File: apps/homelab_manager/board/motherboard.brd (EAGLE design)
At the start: 100 x 80 mm, 39 parts, among them X1 22-23-2021

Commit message: Adding components
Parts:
- removed JP8: UI, pinhead:1X10
- added C3: 100n, rcl:C0805
- added C5: 10u, rcl:C0805
- added C6: 100u, rcl:C0805
- added JP10: LED, pinhead:1X01
- added JP11: 5V, pinhead:1X01
- added JP9: (no value), pinhead:1X11
- added R16: 330, rcl:R0805
- added R17: 5k, rcl:R0805
- added R18: 1k, rcl:R0805
- added R19: 100k, rcl:R0805
- added U$8: MGSF1N03L, bzd:SOT23_3_PIN
- added U$9: LD1117, bzd:SOT223_3_PIN
- R15: value 20k -> 5k
- moved R15 92.1 mm to (85.1, 15.2)
- moved C1 87.6 mm to (77.5, 14.0)
- moved U$2 81.0 mm to (77.5, 33.0)
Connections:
- removed net N$6: C1.1, R15.2, U$2.B1, U$2.B2
- new net 5V: C3.1, C6.1, JP11.1, U$2.A1, U$2.A2, U$2.H1, U$9.P$2
- new net GND_LED: JP9.11, R16.2
- new net LED: JP10.1, R18.1, R19.2
- new net N$14: R16.1, U$8.P$3
- new net N$7: JP9.9
- new net N$8: R18.2, U$8.P$1
- new net VOUT_GAZ: C1.1, R15.2, R17.1, U$1.PIN_22
- net 3.3V: now also JP9.1; no longer JP8.1, JP8.9
- net 7V: now also C5.1, U$9.P$3
- net EINK_BUSY: now also JP9.8; no longer JP8.8
- net EINK_DC: now also JP9.6; no longer JP8.6
- net EINK_RST: now also JP9.7; no longer JP8.7
- net GND: now also C3.2, C5.2, C6.2, JP9.2, R19.1, U$8.P$2, U$9.P$1; no longer JP8.2
- net N$5: now also R17.2, U$2.B1, U$2.B2; no longer U$2.A1, U$2.A2, U$2.H1
- net SPI_CLK: now also JP9.4; no longer JP8.4
- net SPI_CS0: now also JP9.5; no longer JP8.5
- net SPI_MOSI: now also JP9.3; no longer JP8.3
- net SWITCH: now also JP9.10; no longer JP8.10
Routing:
- net GND: track 52.1 -> 68.5 mm
- net LED: track 0.00 -> 8.93 mm
- net 5V: track 0.00 -> 6.17 mm
- net 7V: track 15.5 -> 18.4 mm
- net N$8: track 0.00 -> 2.75 mm
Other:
- outline, holes or cut-outs redrawn

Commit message: Started main layout
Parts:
- removed X1: 22-23-2021, con-molex:22-23-2021
- added C7: 100n, rcl:C0805
- added D4: 1N4148, diode:DO-214AC
- added DCIN, RELAY: 22-23-2021, con-molex:22-23-2021
- added JP12: HOMELAB, pinhead:1X01
- added R21, R24: 100k, rcl:R0805
- added R23: 1k, rcl:R0805
- added U$10: TMP101, bzd:SOT23_6_PIN
- added U$11: MGSF1N03L, bzd:SOT23_3_PIN
- moved R15 62.0 mm to (34.3, 50.8), flipped to the bottom
- moved JP9 60.6 mm to (35.6, 5.08), turned to 0 degrees
- moved C1 57.4 mm to (30.5, 47.0), flipped to the bottom
- moved R14 55.7 mm to (52.1, 5.08)
- moved L3 50.6 mm to (11.7, 23.6), turned to 180 degrees
- moved R17 50.4 mm to (38.1, 47.0), flipped to the bottom
- moved JP6 50.2 mm to (3.81, 25.4), turned to 180 degrees
- moved C3 45.9 mm to (40.6, 50.8), flipped to the bottom
- moved U$4 44.5 mm to (12.7, 26.7), turned to 180 degrees
- moved C11 44.1 mm to (8.89, 27.2), turned to 90 degrees
- moved R9 43.8 mm to (6.35, 27.9), turned to 90 degrees
- moved C10 43.1 mm to (17.8, 27.9), turned to 270 degrees
- moved R18 42.3 mm to (65.3, 25.5)
- moved JP10 42.3 mm to (61.5, 25.0)
- moved R16 42.3 mm to (57.9, 27.3)
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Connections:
- new net GND_RELAY: D4.A, RELAY.1, U$11.P$3
- new net HOMELAB_POWER: JP12.1, R23.1, R24.2, U$1.PIN_21
- new net N$13: R23.2, U$11.P$1
- new net TEMPERATURE_ALERT: R21.1, U$1.PIN_25, U$10.3
- net 12V: now also DCIN.2; no longer X1.2
- net 3.3V: now also C7.1, R21.2, U$10.4
- net GND: now also C7.2, DCIN.1, R24.1, U$10.2, U$10.5, U$11.P$2; no longer X1.1
- net I2C_SCL: now also U$10.1
- net I2C_SDA: now also U$10.6
- net LED: now also U$1.PIN_26
- net VIN_REG: now also D4.C, RELAY.2
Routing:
- net HOMELAB_POWER: track 0.00 -> 8.93 mm
- net GND: track 68.5 -> 77.5 mm
- net 3.3V: track 0.00 -> 4.58 mm
- net GND_RELAY: track 0.00 -> 3.29 mm
- net N$13: track 0.00 -> 2.75 mm
- net TEMPERATURE_ALERT: track 0.00 -> 2.41 mm
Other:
- board size 100 x 80 mm -> 74.6 x 55.9 mm

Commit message: Updated bazelisk + bazel
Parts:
- removed DCIN: 22-23-2021, con-molex:22-23-2021
- added DC_12V: DC_POWER_2.1MM, bzd:DC_POWER_2.1MM
- moved JP2 11.0 mm to (20.2, 38.2)
- moved R4 11.0 mm to (20.2, 42.0)
- moved U$3 11.0 mm to (17.4, 40.5)
- moved C2 11.0 mm to (15.6, 39.0)
- moved R3 11.0 mm to (16.9, 45.8)
- moved U$1 1.49 mm to (38.6, 32.9)
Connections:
- net 12V: now also DC_12V.1; no longer DCIN.2
- net GND: now also DC_12V.2, DC_12V.3; no longer DCIN.1

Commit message: motherboard (wip)
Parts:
- added JP8: SWITCH_LED, pinhead:1X03
- added RELAY1: 22-23-2021, con-molex:22-23-2021
- added U$12, U$13: SCREW_TERMINAL, bzd:SCREW_TERMINAL
- added U$7: RELAY_SONGLE, bzd:RELAY_SONGLE
- JP9: value (none) -> UI
- moved JP9 70.3 mm to (37.9, 75.4)
- moved JP4 54.2 mm to (18.0, 28.3)
- moved JP7 53.9 mm to (19.6, 36.9)
- moved R10 53.9 mm to (23.7, 28.9)
- moved R11 53.9 mm to (23.7, 33.4)
- moved R12 53.9 mm to (19.0, 40.7)
- moved R13 53.9 mm to (15.7, 41.9)
- moved U$6 53.9 mm to (14.5, 36.9)
- moved D3 53.9 mm to (17.0, 33.6)
- moved R14 53.1 mm to (54.1, 58.2)
- moved U$10 31.9 mm to (46.9, 30.8), flipped to the bottom, turned to 90 degrees
- moved R21 31.0 mm to (42.1, 31.6), flipped to the bottom, turned to 90 degrees
- moved C7 27.3 mm to (43.3, 35.4), flipped to the bottom, turned to 180 degrees
- moved C2 24.9 mm to (16.4, 63.9)
- moved DC_12V 24.9 mm to (-2.79, 76.6)
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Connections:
- removed net N$7: JP9.9
- new net N$15: RELAY1.1, U$7.COMMAND_V-
- new net N$16: U$12.P$2, U$13.P$1
- new net N$17: U$12.P$1, U$7.V-
- new net N$18: U$13.P$2, U$7.NO_V+
- new net N$6: RELAY1.2, U$7.COMMAND_V+
- net 3.3V: now also JP9.9
- net FAN2_SENSE: now also U$1.PIN_21; no longer U$1.PIN_18
- net HOMELAB_POWER: now also U$1.PIN_4; no longer U$1.PIN_21
- net LED: now also U$1.PIN_6; no longer U$1.PIN_26
- net VOUT_CURRENT: now also U$1.PIN_18; no longer U$1.PIN_4
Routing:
- net GND: track 77.5 -> 198.3 mm, vias 6 -> 9
- net VIN_REG: track 14.2 -> 130.7 mm, vias 0 -> 2
- net 7V: track 18.4 -> 94.9 mm, vias 0 -> 2
- net 3.3V: track 4.58 -> 49.4 mm, vias 0 -> 1
- net FAN1_SENSE: track 0.00 -> 38.5 mm, vias 0 -> 1
- net SWITCH: track 0.00 -> 36.8 mm, vias 0 -> 1
- net FAN_SWITCH: track 17.9 -> 53.5 mm, vias 0 -> 2
- net I2C_SCL: track 0.00 -> 35.4 mm, vias 0 -> 2
- net SPI_CS0: track 0.00 -> 34.2 mm, vias 0 -> 1
- net SPI_CLK: track 0.00 -> 32.6 mm, vias 0 -> 1
- net EINK_DC: track 0.00 -> 27.9 mm, vias 0 -> 1
- net SPI_MOSI: track 0.00 -> 27.0 mm
- net I2C_SDA: track 0.00 -> 25.6 mm
- net 5V: track 6.17 -> 30.9 mm
- net FAN2_SENSE: track 0.00 -> 24.7 mm
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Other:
- board size 74.6 x 55.9 mm -> 74.6 x 80.4 mm
- board text added: "230V"
- board text added: "5V"
- board text added: "DANGER! HIGH VOLT"

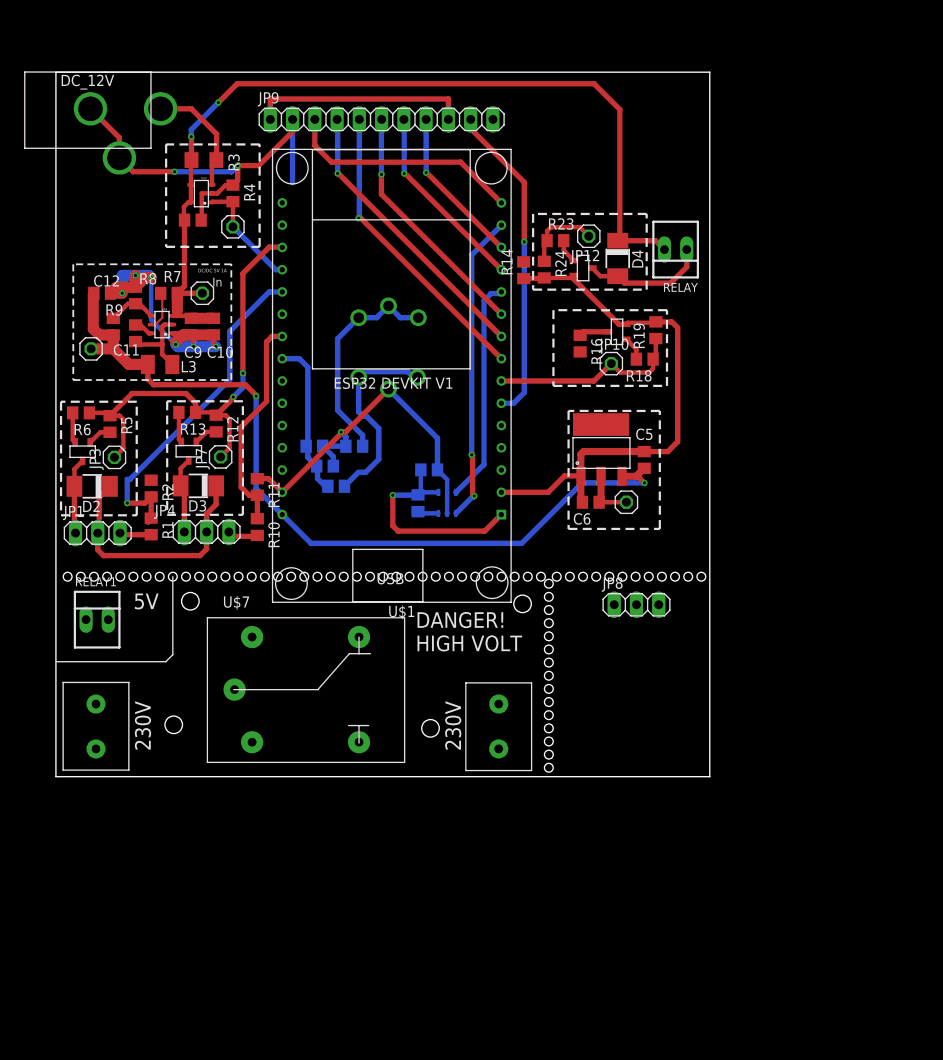
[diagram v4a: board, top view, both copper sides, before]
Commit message: Completed layout rev 1
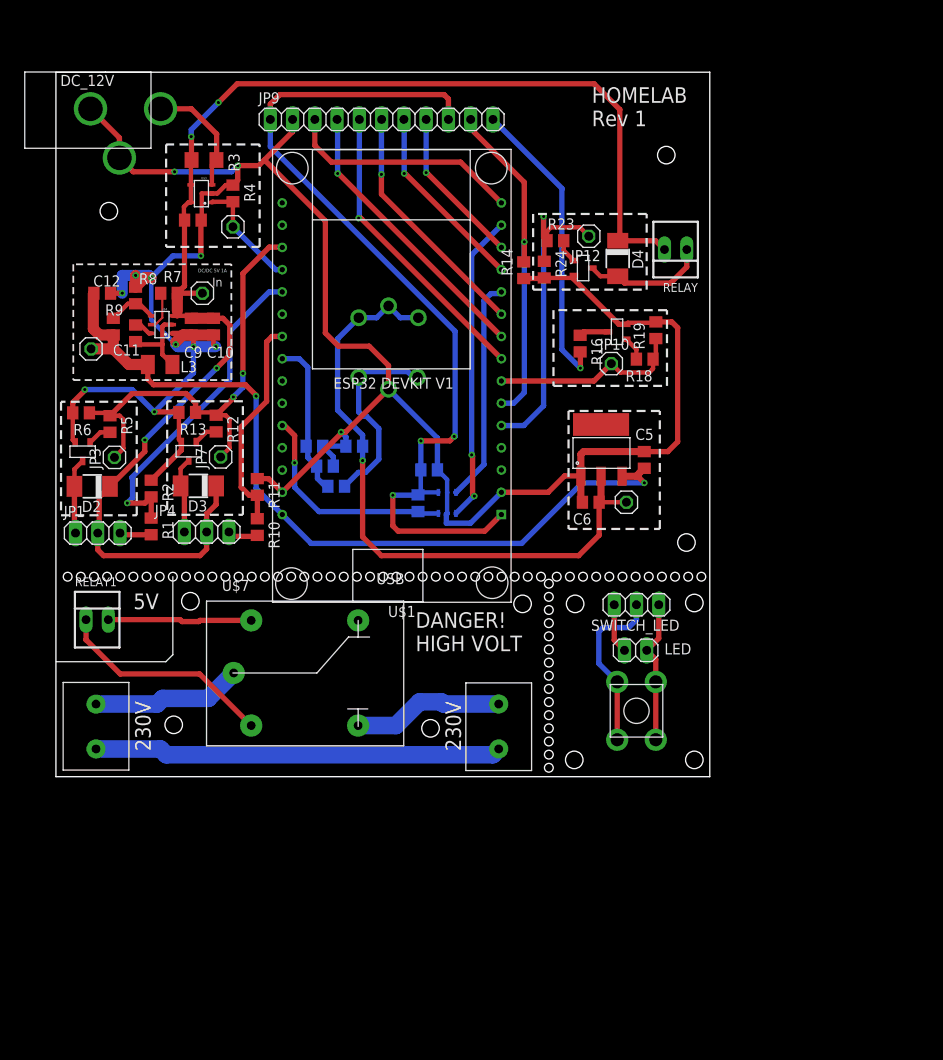
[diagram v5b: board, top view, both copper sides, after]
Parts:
- added LED: LED, pinhead:1X02
- added U$14: MOMENTARY_SWITCH, bzd:MOMENTARY_SWITCH
- moved U$7 1.90 mm to (23.0, 18.2)
- renumbered JP8 to SWITCH_LED
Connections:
- new net N$19: LED.2, SWITCH_LED.1
- new net N$20: SWITCH_LED.2, U$14.A1, U$14.A2
- new net N$7: LED.1, SWITCH_LED.3, U$14.B1, U$14.B2
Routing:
- net GND: track 198.3 -> 270.7 mm, vias 9 -> 12
- net 3.3V: track 49.4 -> 102.6 mm, vias 1 -> 3
- net N$16: track 0.00 -> 46.5 mm
- net 5V: track 30.9 -> 73.9 mm, vias 0 -> 1
- net GND_LED: track 0.00 -> 34.4 mm, vias 0 -> 1
- net HOMELAB_POWER: track 8.93 -> 39.2 mm, vias 0 -> 1
- net VIN_REG: track 130.7 -> 157.5 mm, vias 2 -> 4
- net N$15: track 0.00 -> 25.2 mm
- net TEMPERATURE_ALERT: track 2.41 -> 25.4 mm, vias 0 -> 1
- net N$20: track 0.00 -> 19.7 mm
- net N$18: track 0.00 -> 17.3 mm
- net N$17: track 0.00 -> 17.2 mm
- net N$6: track 0.00 -> 16.5 mm
- net N$7: track 0.00 -> 16.4 mm
- net N$19: track 0.00 -> 5.68 mm
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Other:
- board text added: "HOMELAB Rev 1"
